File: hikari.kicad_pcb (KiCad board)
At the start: 2 copper layers, 44 parts, among them CN1 USB-Micro, IC1 PAM2804AAB010, IC2 PAM2804AAB010, IC3 PAM2804AAB010, IC4 PAM2804AAB010, IC5 ESP-12F, IC6 CH340G, T1 AO3401

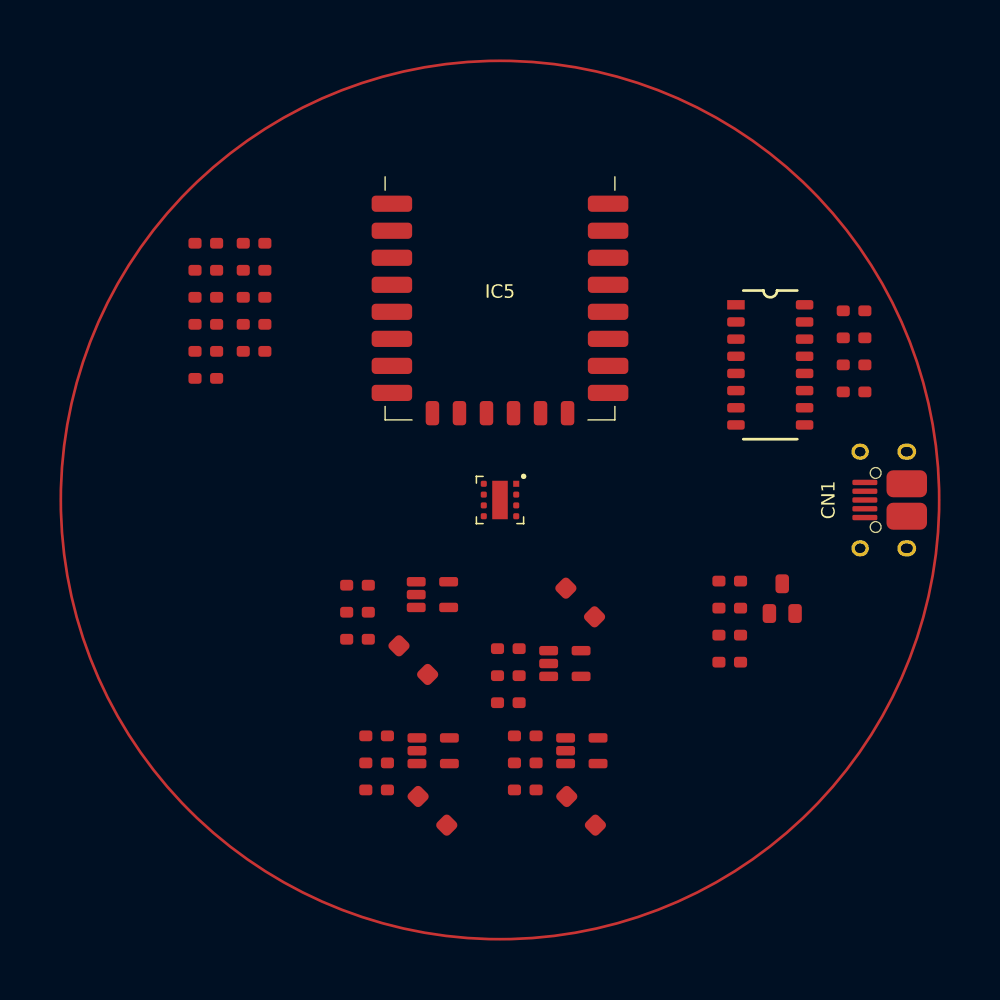
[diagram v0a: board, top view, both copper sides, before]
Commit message: worked layout, fixed 3V3 being GND net
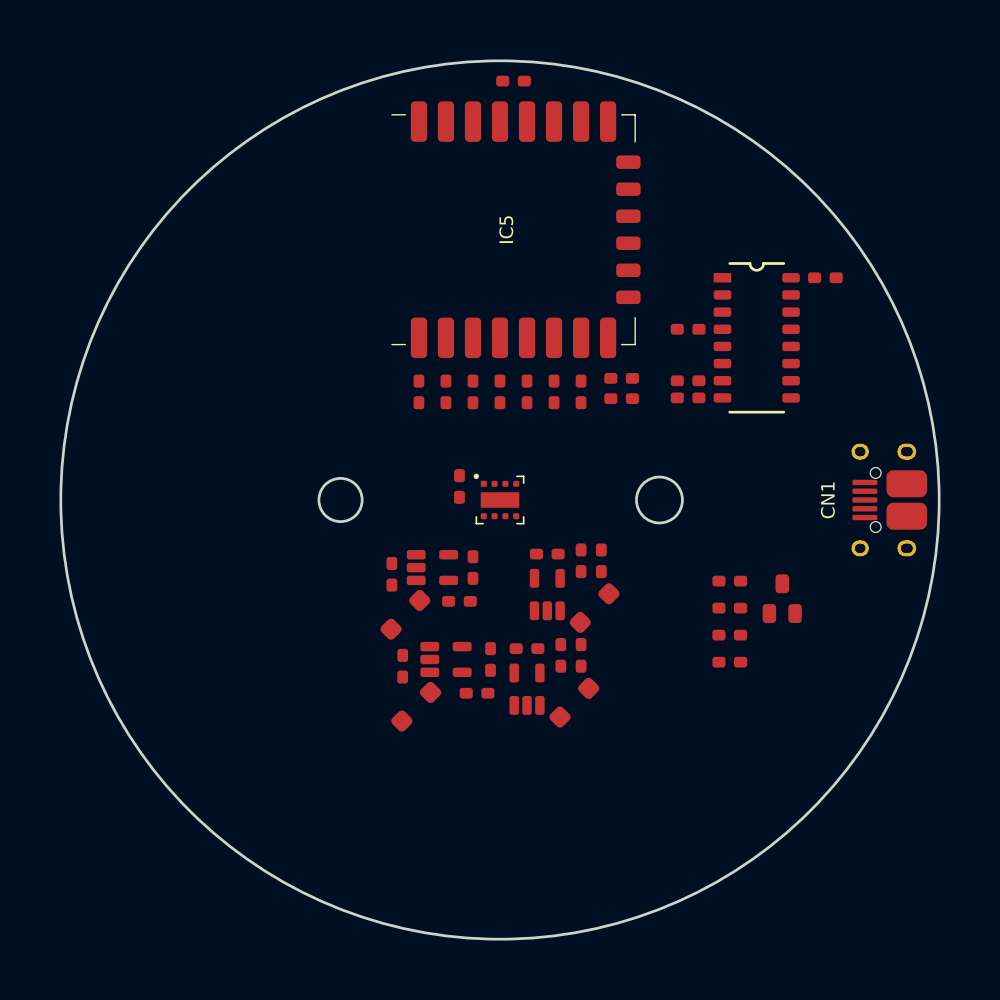
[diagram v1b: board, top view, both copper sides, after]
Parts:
- moved C11 32.8 mm to (161.4, 94.1)
- moved C12 31.8 mm to (161.4, 92.6)
- moved R8 31.7 mm to (153.4, 70.6), turned to 180 degrees
- moved R10 25.8 mm to (158.4, 93.6), turned to 90 degrees
- moved NTC1 23.4 mm to (149.4, 100.6), turned to 90 degrees
- moved R11 23.3 mm to (156.4, 93.6), turned to 90 degrees
- moved R9 23.0 mm to (154.4, 93.6), turned to 90 degrees
- moved R6 20.4 mm to (150.4, 93.6), turned to -90 degrees
- moved R12 18.9 mm to (152.4, 93.6), turned to 90 degrees
- moved R4 17.5 mm to (155.9, 105.6), turned to 180 degrees
- moved C6 16.9 mm to (158.4, 113.1), turned to 90 degrees
- moved R7 16.1 mm to (146.4, 93.6), turned to 90 degrees
- moved C8 16.0 mm to (159.9, 106.1), turned to 90 degrees
- moved C5 15.9 mm to (156.9, 113.1), turned to 90 degrees
- moved L4 15.0 mm to (159.4, 109.6), turned to 90 degrees
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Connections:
- C10 pad 1: GND -> 3V3
- C11 pad 1: GND -> 3V3
- C12 pad 1: GND -> 3V3
- C13 pad 1: GND -> 3V3
- IC5 pad 8: GND -> 3V3
- IC6 pad 4: GND -> 3V3
- R14 pad 2: GND -> 3V3
- R6 pad 2: GND -> 3V3
- R7 pad 1: GND -> 3V3
- R8 pad 2: GND -> 3V3
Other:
- board outline added: 65 x 65 mm

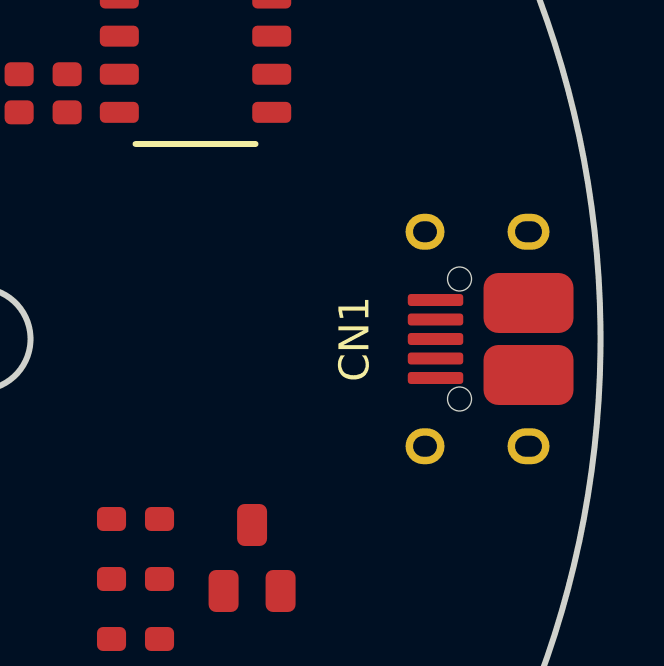
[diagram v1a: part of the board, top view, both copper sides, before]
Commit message: added type-c connector
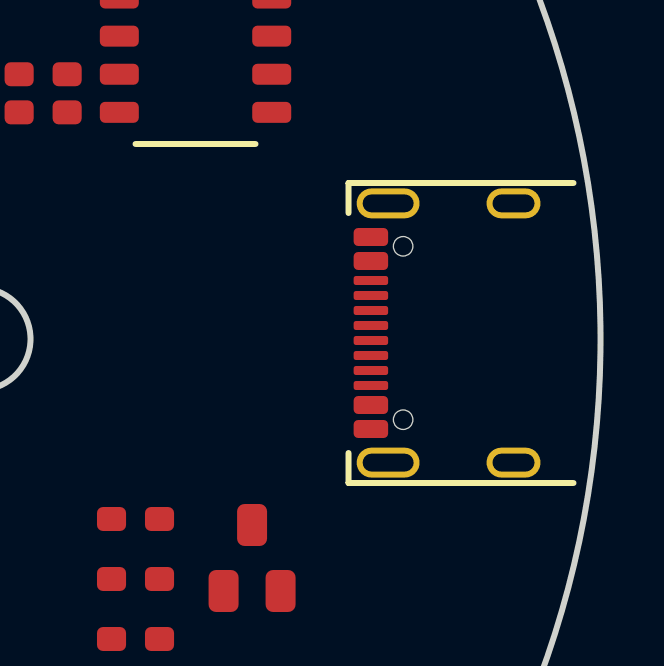
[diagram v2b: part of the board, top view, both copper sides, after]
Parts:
- CN1: value USB-Micro -> USB-C; footprint USB:micro_usb -> USB:USB4105-GF-A
- moved CN1 1.81 mm to (182.0, 101.4)
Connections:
- IC6 pad 5: Net-(CN1-DP) -> Net-(CN1-D1P)
- IC6 pad 6: Net-(CN1-DN) -> Net-(CN1-D1N)

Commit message: did most of todo items
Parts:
- added BAT1: Battery, pin_headers:Battery_solder-points, F.Cu at (152.4, 129.8)
- added CN2: 1x3, pin_headers:1x3, F.Cu at (167.4, 79.6)
- added IC7: AP2112K-3.3TRG1, SOT:SOT-23-5, F.Cu at (173.4, 109.6)
- added R13: 5k1, SMT:0603, F.Cu at (174.4, 102.6)
- added R15: 5k1, SMT:0603, F.Cu at (174.4, 98.6)
- added R16: 10k, SMT:0603, F.Cu at (176.4, 109.6)
- added SW1: LS12W3-T, buttons:LS12W3-T, F.Cu at (181.8, 92.2)
- added SW2: JS102011SAQN, buttons:JS102011SAQN, F.Cu at (180.2, 113.2)
- added x1: 12MHZ, xtal:3.2x2.5CXO, F.Cu at (166.9, 92.8)
- D2: value D -> SK22A; footprint SMT:0603 -> do:DO-214AC
- T1: value AO3401 -> GSF2301
- moved R8 31.2 mm to (178.2, 89.6), turned to 90 degrees
- moved T1 6.43 mm to (168.9, 113.6), turned to 90 degrees
- moved C9 6.10 mm to (172.9, 112.6)
- moved C10 5.00 mm to (173.4, 106.6), turned to 180 degrees
- moved D2 4.00 mm to (169.4, 107.6), turned to -90 degrees
- moved R9 4.00 mm to (158.4, 93.6)
- moved R5 3.64 mm to (172.9, 114.6), turned to 180 degrees
- moved R10 2.00 mm to (156.4, 93.6)
- moved R11 2.00 mm to (154.4, 93.6)
- moved C16 1.67 mm to (164.7, 92.8), turned to -90 degrees
- moved C15 1.66 mm to (166.9, 95.6)
- moved C14 1.00 mm to (177.5, 85.2)
- moved IC6 1.00 mm to (172.4, 89.6)
- moved C13 0.59 mm to (166.9, 88.8)
- moved CN1 0.22 mm to (181.9, 101.6)
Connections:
- CN1 pad A5: unconnected-(CN1-CC1-PadA5) -> Net-(CN1-CC1)
- CN1 pad A6: Net-(CN1-D1P) -> /USB/DP
- CN1 pad A7: Net-(CN1-D1N) -> /USB/DN
- CN1 pad B5: unconnected-(CN1-CC2-PadB5) -> Net-(CN1-CC2)
- CN1 pad B6: unconnected-(CN1-DP2-PadB6) -> /USB/DP
- CN1 pad B7: unconnected-(CN1-DN2-PadB7) -> /USB/DN
- IC1 pad 1: /MCU/RED -> /RED
- IC2 pad 1: /GREEN/EN -> /GREEN
- IC3 pad 1: /BLUE/EN -> /BLUE
- IC4 pad 1: /MCU/WHITE -> /WHITE
- IC5 pad 10: /BLUE/EN -> unconnected-(IC5-IO15-Pad10)
- IC5 pad 11: /MCU/Button_2 -> /MCU/LED_strip
- IC5 pad 4: /MCU/WHITE -> /RED
- IC5 pad 5: /GREEN/EN -> /GREEN
- IC5 pad 6: unconnected-(IC5-IO12-Pad6) -> /BLUE
- IC5 pad 7: /MCU/RED -> /WHITE
- IC6 pad 5: Net-(CN1-D1P) -> /USB/DP
- IC6 pad 6: Net-(CN1-D1N) -> /USB/DN
- R10 pad 2: /MCU/RED -> /BLUE
- R11 pad 2: /BLUE/EN -> /GREEN
- R12 pad 2: /MCU/WHITE -> /RED
- R9 pad 2: /GREEN/EN -> /WHITE
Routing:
- added copper zone on B.Cu, net GND
- added copper zone on F.Cu, net GND
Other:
- outline, holes or cut-outs redrawn

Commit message: rough layout done
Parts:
- added REF**: M3.5, PCB:M3.5, F.Cu at (179.9, 101.6)
- added REF**: M3.5, PCB:M3.5, F.Cu at (140.4, 101.6)
- added REF**: M3.5, PCB:M3.5, F.Cu at (124.9, 101.6)
- added REF**: M3.5, PCB:M3.5, F.Cu at (164.4, 101.6)
- moved R8 31.5 mm to (152.4, 71.6), turned to 180 degrees
- moved C10 24.0 mm to (152.9, 119.1), turned to 90 degrees
- moved SW1 23.6 mm to (179.8, 115.7), turned to -27.269 degrees
- moved SW2 23.1 mm to (163.9, 129.5), turned to 22.7 degrees
- moved CN1 22.6 mm to (173.3, 122.5), turned to 45 degrees
- moved C14 21.0 mm to (173.8, 105.8), turned to -90 degrees
- moved C13 20.3 mm to (163.9, 109.0)
- moved C15 20.2 mm to (163.9, 115.6)
- moved IC6 20.2 mm to (169.4, 109.6)
- moved C16 20.2 mm to (161.4, 112.8)
- moved R15 20.2 mm to (166.4, 117.1), turned to 0 degrees
- moved x1 20.1 mm to (163.9, 112.8)
- moved R5 20.0 mm to (155.9, 125.1), turned to 0 degrees
- moved IC7 19.9 mm to (155.9, 119.1), turned to 180 degrees
- moved R16 19.0 mm to (159.4, 118.1), turned to 180 degrees
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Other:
- outline, holes or cut-outs redrawn
- board text added: "⌀ 3.5 mm"
- board text added: "⌀ 6 mm"

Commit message: all signals routed
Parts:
- moved NTC1 3.58 mm to (146.2, 99.1)
- moved C12 1.41 mm to (162.4, 94.6), turned to -90 degrees
- moved C11 1.12 mm to (164.4, 94.6), turned to -90 degrees
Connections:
- D1 pad 0: (no net) -> GND
- SW1 pad 0: (no net) -> GND
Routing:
- net 3V3: track 0.00 -> 114.1 mm, vias 0 -> 4
- net 5V: track 0.00 -> 94.9 mm, vias 0 -> 1
- net /MCU/Button_1: track 0.00 -> 59.4 mm
- net /MCU/TX: track 0.00 -> 52.6 mm
- net /MCU/RX: track 0.00 -> 44.4 mm
- net /Power supply/V_USB: track 0.00 -> 37.1 mm, vias 0 -> 4
- net /RED: track 0.00 -> 27.7 mm, vias 0 -> 2
- net /GREEN: track 0.00 -> 27.1 mm, vias 0 -> 2
- net /BLUE: track 0.00 -> 25.2 mm, vias 0 -> 2
- net /WHITE: track 0.00 -> 24.4 mm, vias 0 -> 2
- net Net-(D1B-A): track 0.00 -> 24.1 mm, vias 0 -> 2
- net Net-(D1C-A): track 0.00 -> 23.3 mm, vias 0 -> 2
- net Net-(D1A-A): track 0.00 -> 22.4 mm, vias 0 -> 2
- net Net-(D1D-A): track 0.00 -> 21.3 mm, vias 0 -> 2
- net /MCU/LED_strip: track 0.00 -> 15.0 mm
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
